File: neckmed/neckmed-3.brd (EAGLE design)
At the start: 42 x 24.9 mm, 9 parts, among them U1 HT7333, U2 GY-521MPU6050

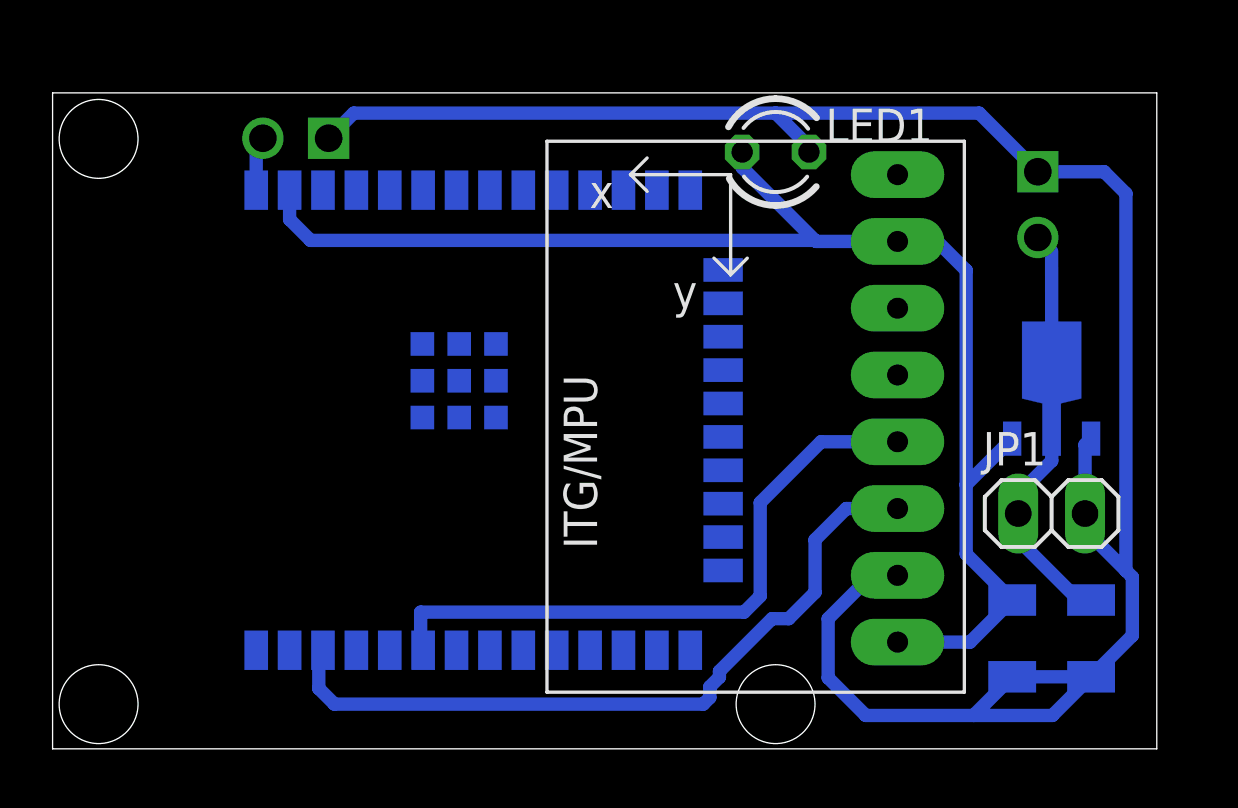
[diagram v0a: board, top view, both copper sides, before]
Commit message: minus esp clearance
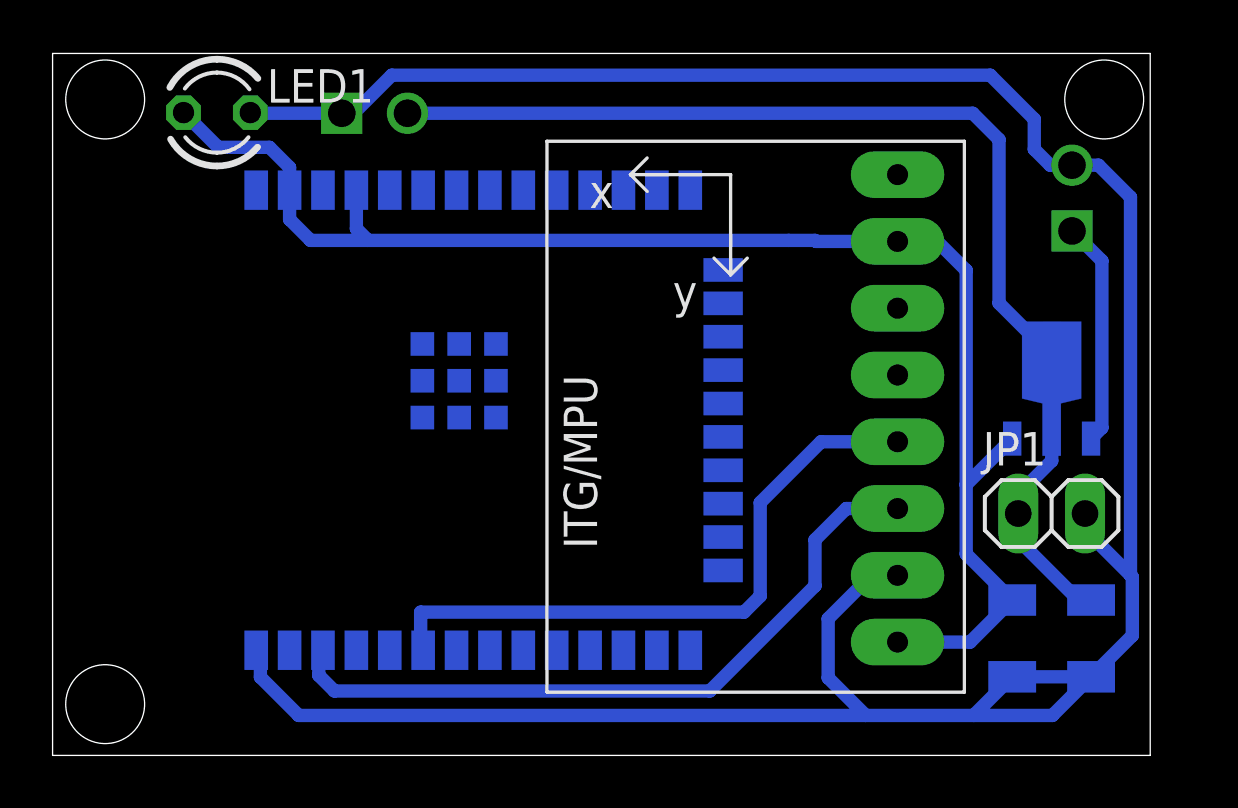
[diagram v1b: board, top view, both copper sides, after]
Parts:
- moved SW 29.1 mm to (38.2, 21.0), turned to 270 degrees
- moved CHARGER 26.1 mm to (12.2, 24.8), turned to 0 degrees
- moved LED1 21.3 mm to (6.25, 24.2)
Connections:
- net GND: now also SW.2, U$1.38; no longer SW.1, U1.1
- net N$2: now also SW.1, U1.1; no longer SW.2, U$1.1
- net VCC: now also U$1.4
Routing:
- net N$1: track 15.2 -> 43.2 mm
- net GND: track 80.7 -> 105.2 mm
- net N$2: track 2.08 -> 8.54 mm
- net VCC: track 52.9 -> 56.3 mm
- net N$8: track 28.4 -> 27.2 mm
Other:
- board size 42 x 24.9 mm -> 41.8 x 26.7 mm

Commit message: move switch
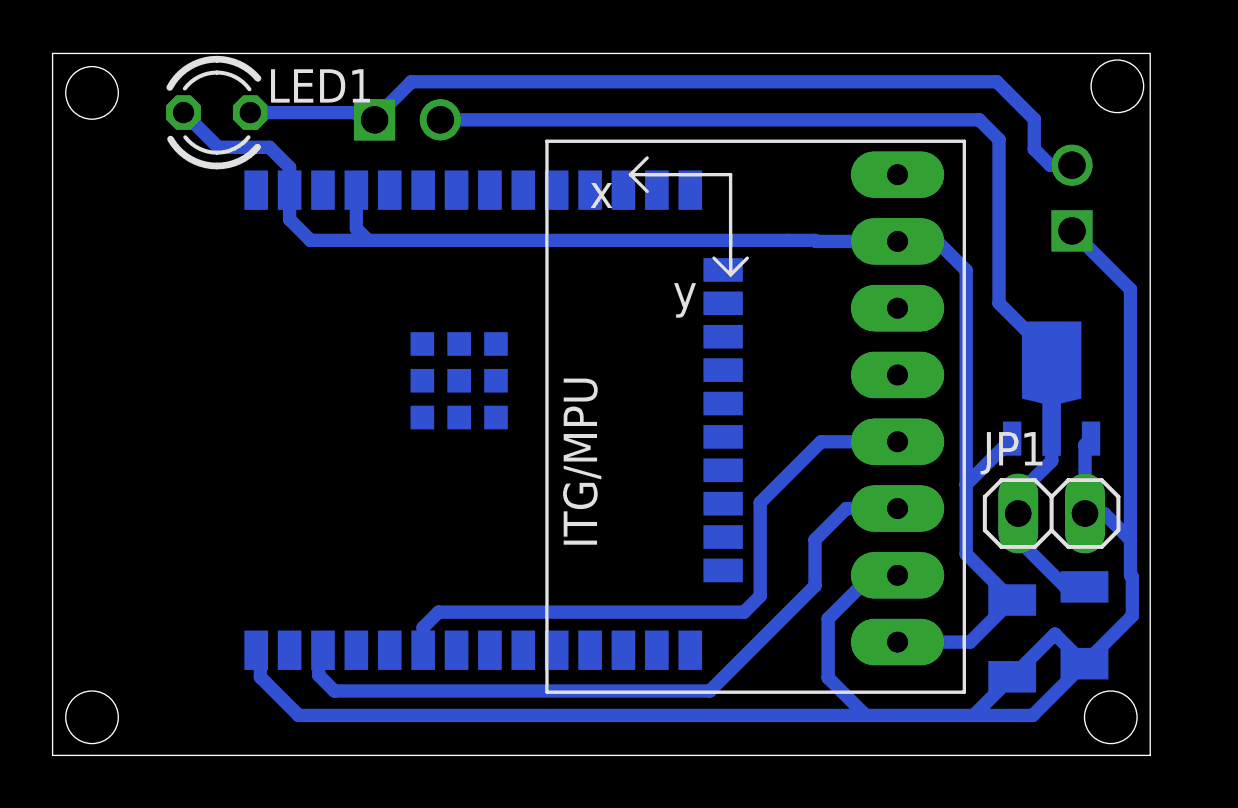
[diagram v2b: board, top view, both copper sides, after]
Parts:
- moved CHARGER 1.27 mm to (13.5, 24.5)
- moved C3 0.56 mm to (39.2, 4.75)
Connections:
- net GND: now also SW.1, U1.1; no longer CHARGER.1, LED1.K, SW.2
- net N$2: now also CHARGER.1, LED1.K, SW.2; no longer SW.1, U1.1
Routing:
- net GND: track 105.2 -> 71.3 mm
- net N$2: track 8.54 -> 34.0 mm
- net N$1: track 43.2 -> 41.4 mm

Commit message: update xh library
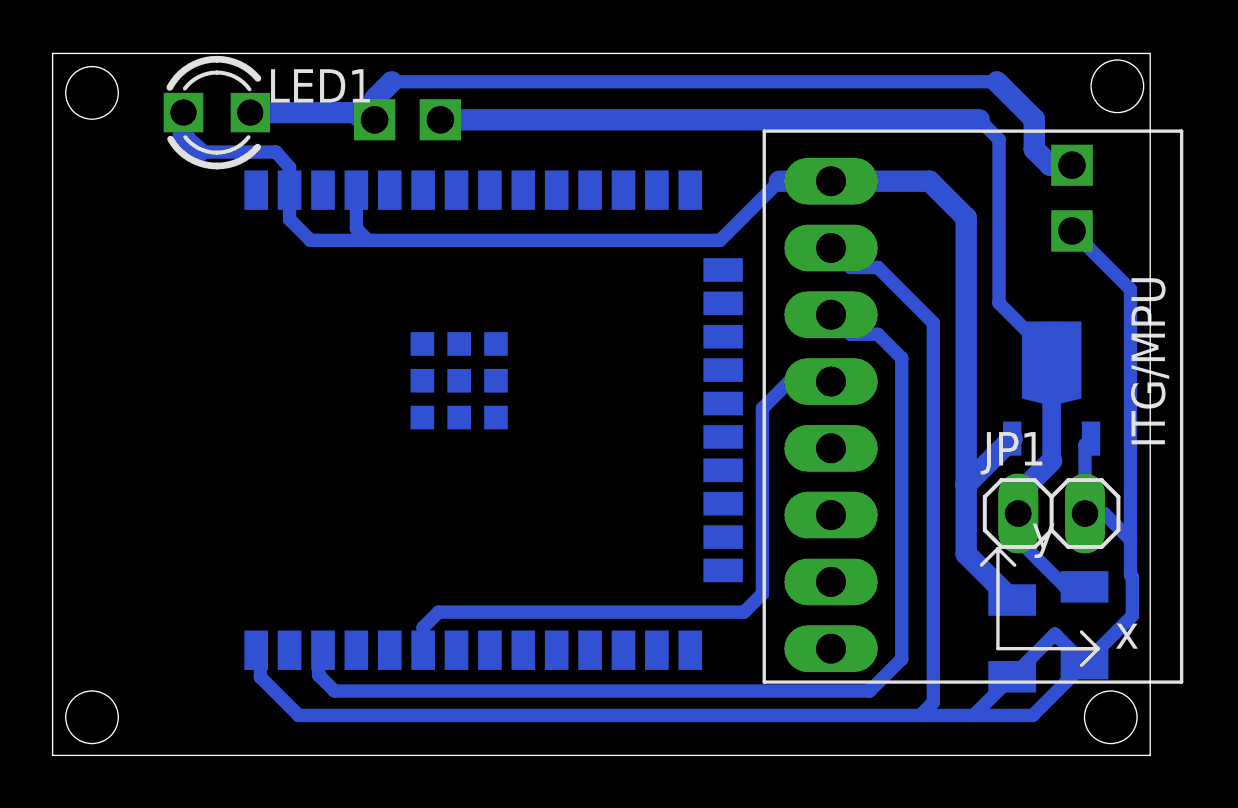
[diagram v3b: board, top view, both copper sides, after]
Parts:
- moved U2 15.3 mm to (38.5, 12.8), turned to 0 degrees
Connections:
- net VCC: no longer U2.ADO
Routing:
- net GND: track 71.3 -> 83.3 mm
- net N$8: track 27.2 -> 38.8 mm
- net VCC: track 56.3 -> 54.9 mm
